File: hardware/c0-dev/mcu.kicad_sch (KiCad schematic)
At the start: 51 parts, among them J16 TAG_CONNECT, J17 PinHeader_2.54mm, U10 RP2350A, U7 TCA9555PWR, U8 W25Q128JVP, U9 TPS3820-33DBV, Y1 ABM8-272-T3 (12Mhz)

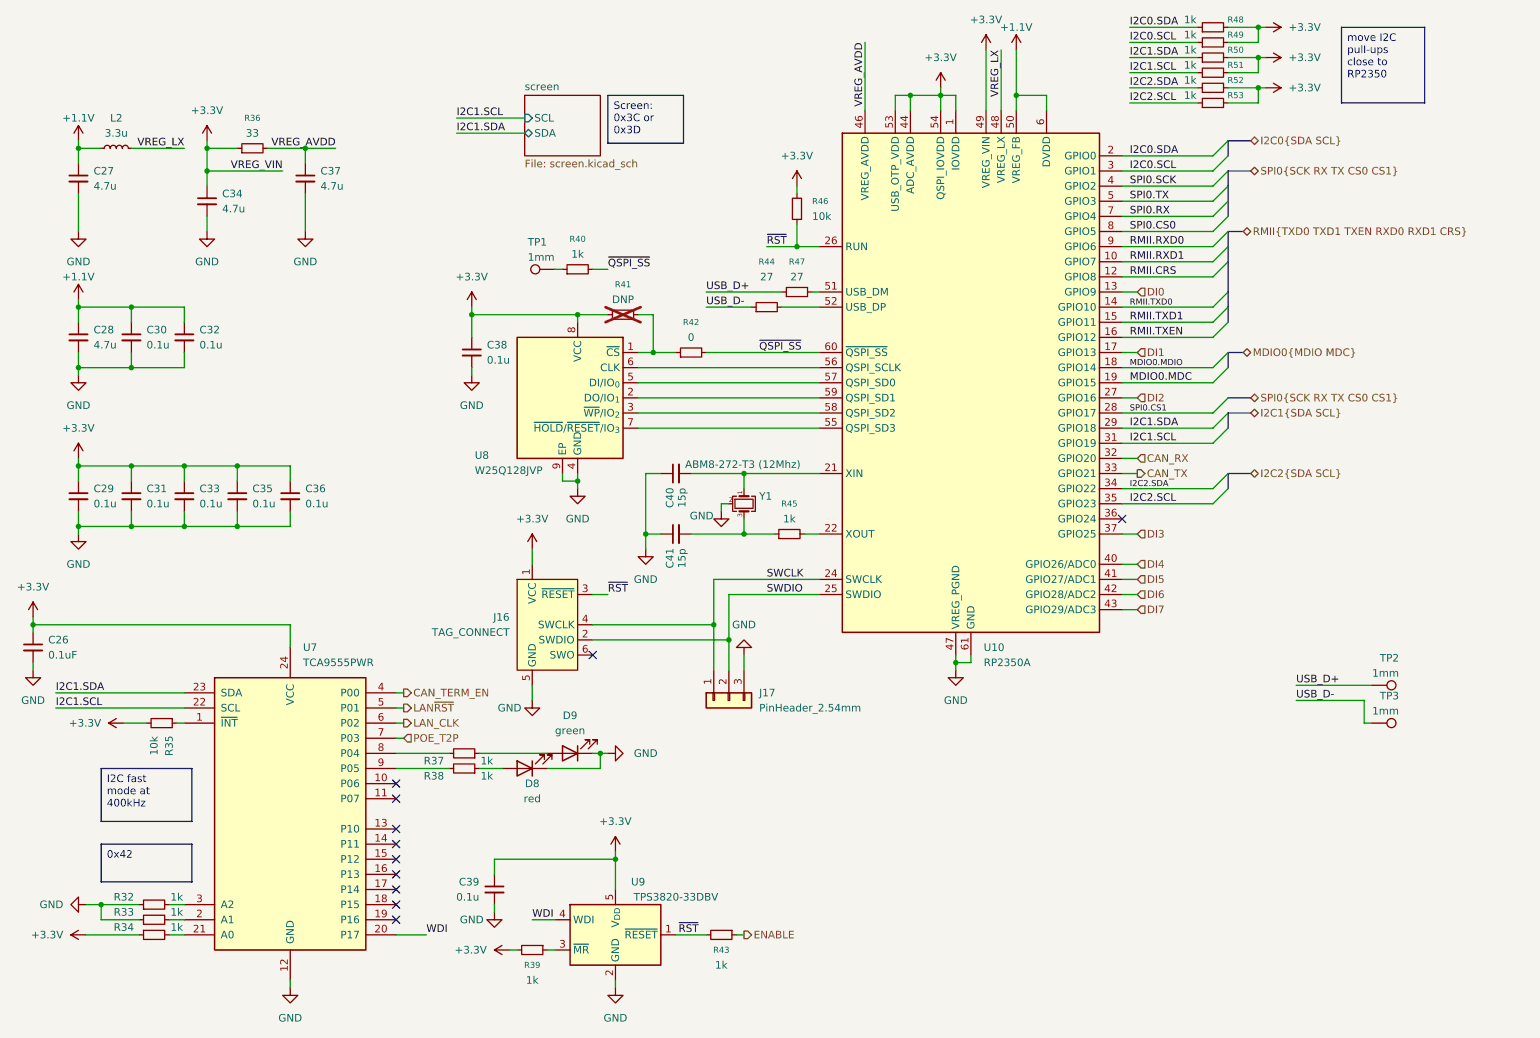
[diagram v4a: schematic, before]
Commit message: page based annotation + flybuck fb
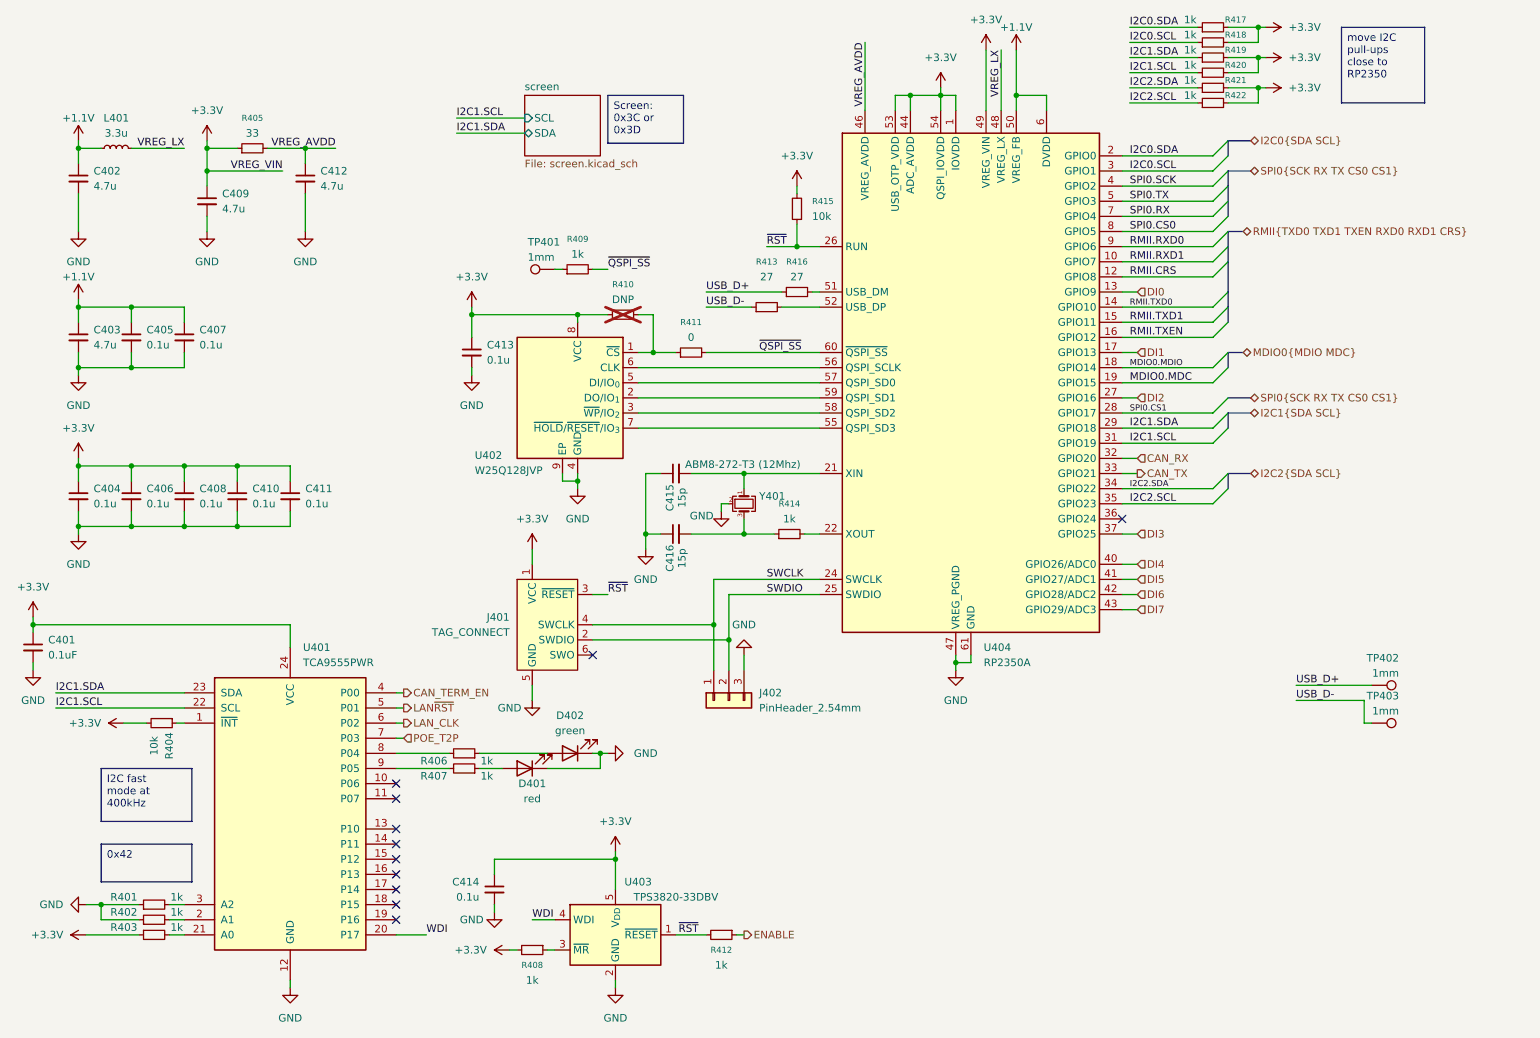
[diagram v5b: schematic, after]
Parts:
- renumbered C26 to C401, C27 to C402, C28 to C403, C29 to C404, C30 to C405, C31 to C406, C32 to C407, C33 to C408, C34 to C409, C35 to C410, C36 to C411, C37 to C412, C38 to C413, C39 to C414, C40 to C415, C41 to C416, D8 to D401, D9 to D402, J16 to J401, J17 to J402, L2 to L401, R32 to R401, R33 to R402, R34 to R403, R35 to R404, R36 to R405, R37 to R406, R38 to R407, R39 to R408, R40 to R409, R41 to R410, R42 to R411, R43 to R412, R44 to R413, R45 to R414, R46 to R415, R47 to R416, R48 to R417, R49 to R418, R50 to R419, R51 to R420, R52 to R421, R53 to R422, TP1 to TP401, TP2 to TP402, TP3 to TP403, U7 to U401, U8 to U402, U9 to U403, U10 to U404, Y1 to Y401

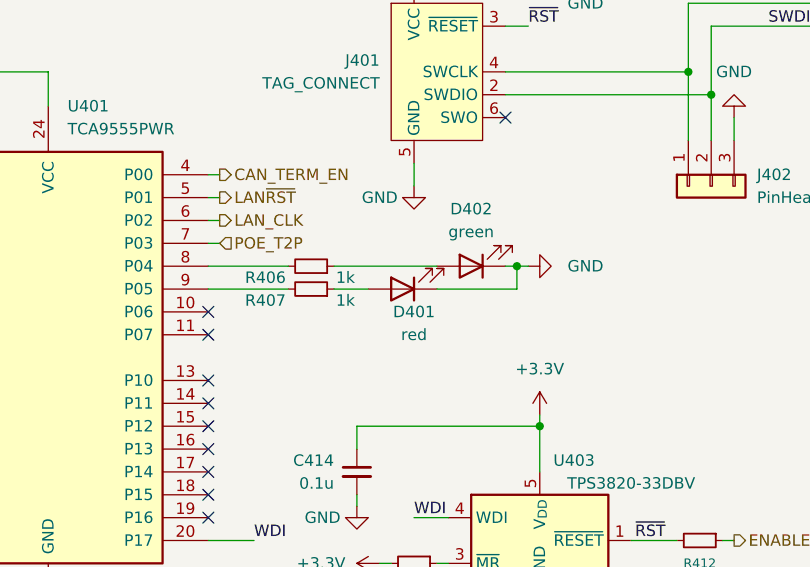
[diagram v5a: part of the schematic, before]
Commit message: power and isolation cleanup
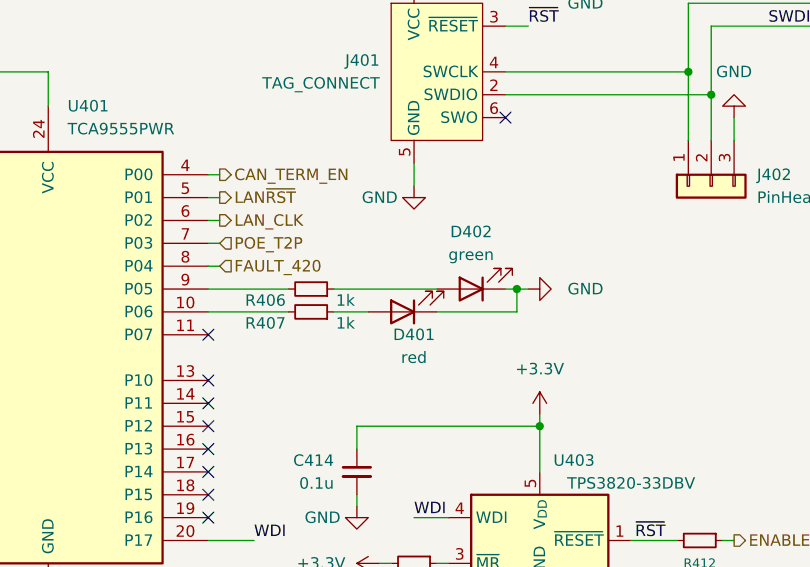
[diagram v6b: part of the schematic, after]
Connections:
- net at U401.10 (P06): now also R407.2
- net at R406.2: now also U401.9 (P05); no longer U401.8 (P04)
- new net FAULT_420: U401.8 (P04)
- no-connect marks 11 -> 10

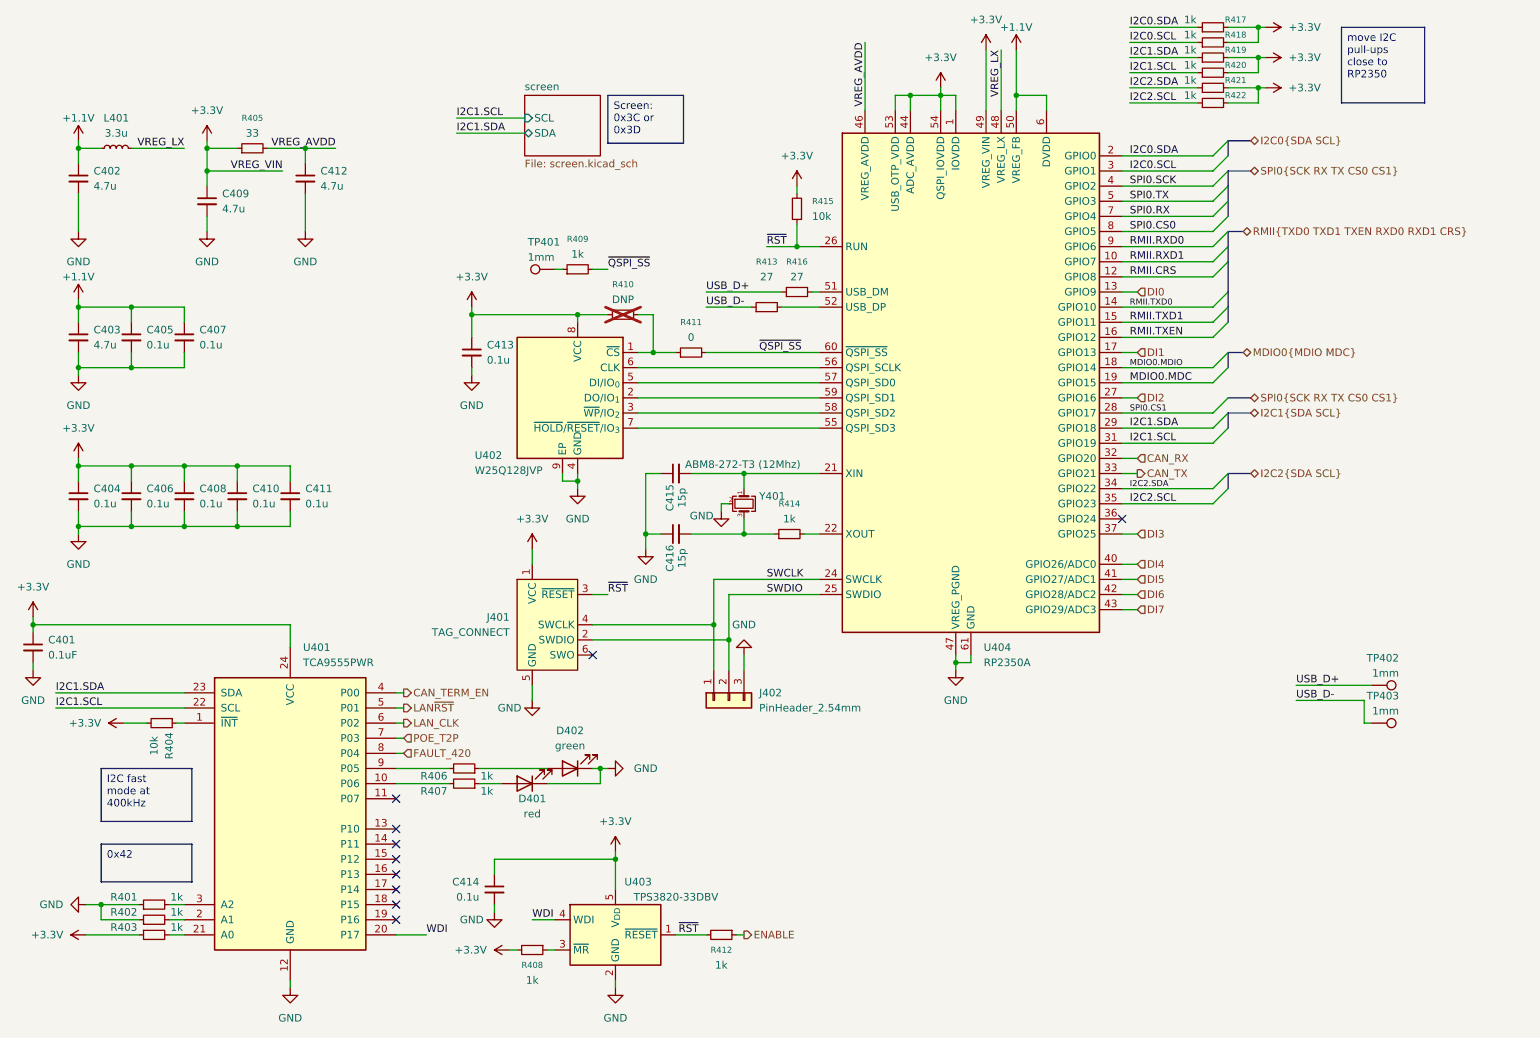
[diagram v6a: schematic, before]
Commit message: added LEDs
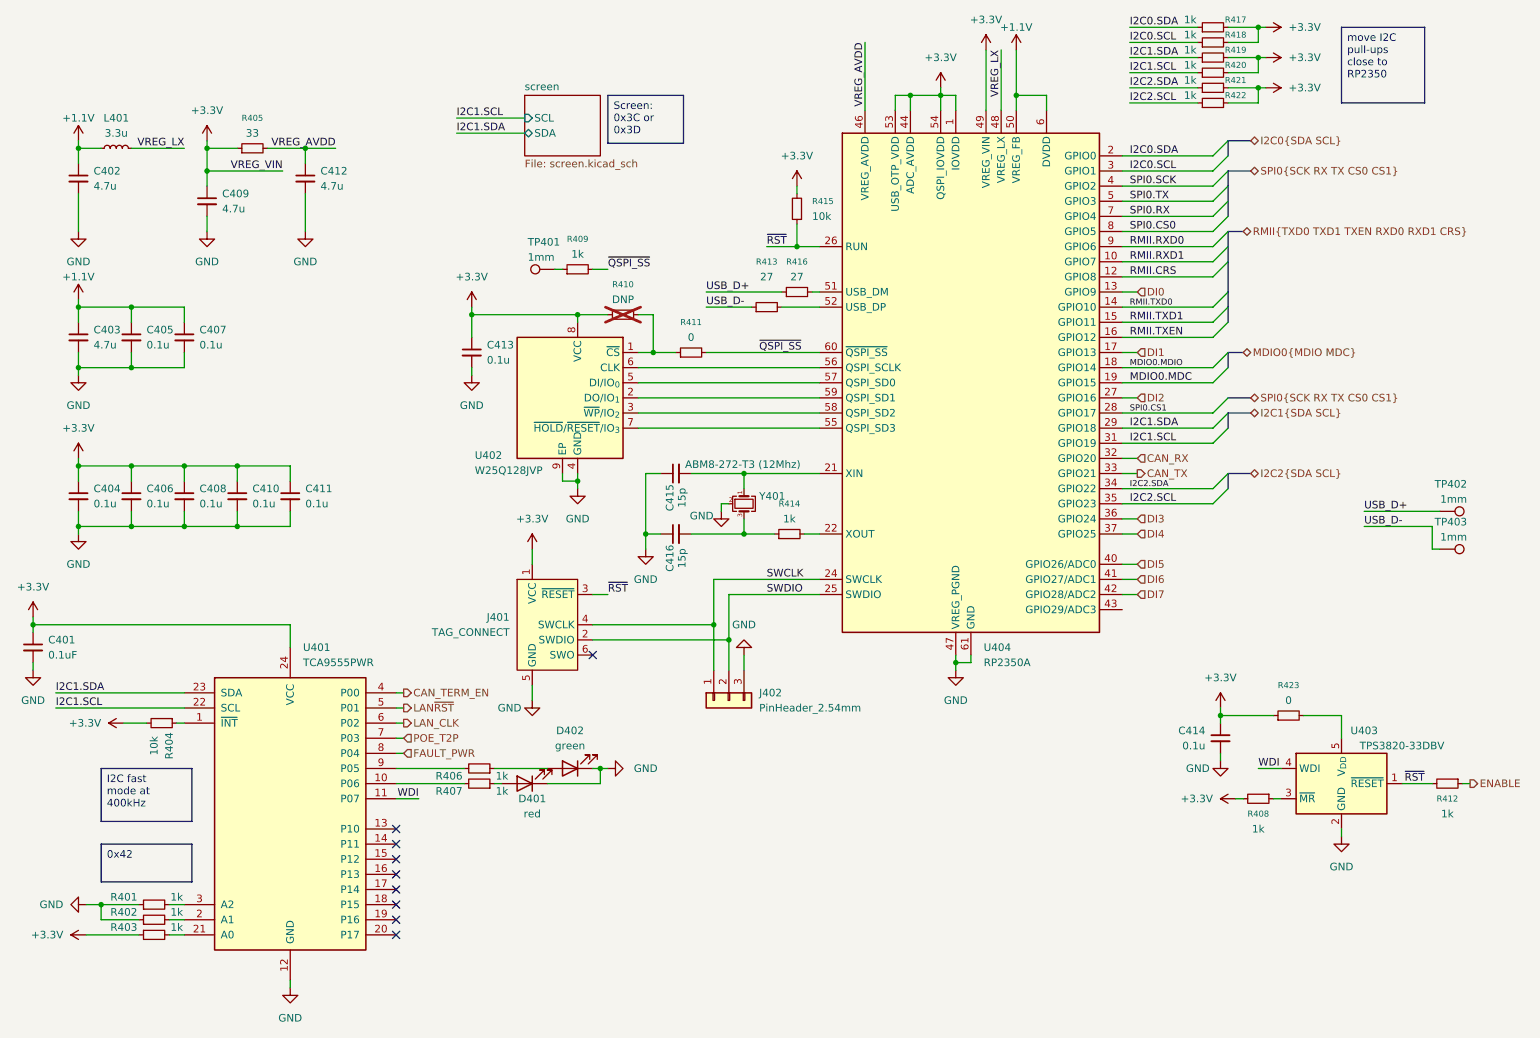
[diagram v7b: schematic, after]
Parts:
- added R423: 0, Resistor_SMD:R_0402_1005Metric, symbol Device:R_Small
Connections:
- net +3.3V: now also R423.1; no longer U403.5 (V_{DD})
- net DI3: now also U404.36 (GPIO24); no longer U404.37 (GPIO25)
- net DI4: now also U404.37 (GPIO25); no longer U404.40 (GPIO26/ADC0)
- net DI5: now also U404.40 (GPIO26/ADC0); no longer U404.41 (GPIO27/ADC1)
- net DI6: now also U404.41 (GPIO27/ADC1); no longer U404.42 (GPIO28/ADC2)
- net DI7: now also U404.42 (GPIO28/ADC2); no longer U404.43 (GPIO29/ADC3)
- net WDI: now also U401.11 (P07); no longer U401.20 (P17)
- net FAULT_420 renamed FAULT_PWR
- new net: R423.2, U403.5 (V_{DD})
- no-connect marks 10 -> 9
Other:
- moved on the sheet: C414, R406, R407, R408, R412, TP402, TP403, U403

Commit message: rgb's and 70x160mm
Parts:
- renumbered C415 to C414, C416 to C415, C414 to C416, R409 to R408, R410 to R409, R411 to R410, R413 to R411, R414 to R412, R415 to R413, R416 to R414, R417 to R415, R418 to R416, R419 to R417, R420 to R418, R421 to R419, R422 to R420, R408 to R421, R423 to R422, R412 to R423, U404 to U403, U403 to U404
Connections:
- net RGBs: now reaches U403.43 (GPIO29/ADC3)
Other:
- sheet screen renamed indicators
- sheet indicators: file screen.kicad_sch -> indicators.kicad_sch
- sheet indicators ports: added LED; removed none
